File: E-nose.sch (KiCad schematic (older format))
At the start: 34 parts, among them T1 Temp_si072, U1 TCA9548APWR, U3 RTC_DS3231

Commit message: Final with Gerbers
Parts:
- removed XA2: Arduino_Due_Shield, Arduino:Arduino_Due_Shield, symbol arduino:Arduino_Due_Shield
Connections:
- wire segments 80 -> 81
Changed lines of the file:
@@
 $EndDescr
-$Comp
-L arduino:Arduino_Due_Shield XA2
-U 1 1 620C63F8
-P 6450 8400
-F 0 "XA2" H 6450 6019 60  0000 C CNN
-F 1 "Arduino_Due_Shield" H 6450 5913 60  0000 C CNN
-F 2 "Arduino:Arduino_Due_Shield" H 7150 11150 60  0001 C CNN
-F 3 "https://store.arduino.cc/arduino-due" H 7150 11150 60  0001 C CNN
-	1    6450 8400
-	1    0    0    -1
-$EndComp
 $Comp
 L Interface_Expansion:TCA9548APWR U1
@@
 	13300 1650 13350 1650
 Text GLabel 11750 3000 0    50   Input ~ 0
-SD4
+SD1
 $Comp
 L power:VCC #PWRVcc0104
@@
 	11650 2700 11800 2700
 Text GLabel 11750 2800 0    50   Input ~ 0
-SC4
+SC1
 Wire Wire Line
 	11800 3000 11750 3000
@@
 	11750 2800 11800 2800
 Text GLabel 13350 3050 0    50   Input ~ 0
-SD2
+SD3
 $Comp
 L power:VCC #PWRVcc0105
@@
 	13250 2750 13400 2750
 Text GLabel 13350 2850 0    50   Input ~ 0
-SC2
+SC3
 Wire Wire Line
 	13400 3050 13350 3050
@@
 	13350 2850 13400 2850
 Text GLabel 11750 4200 0    50   Input ~ 0
-SD1
+SD5
 $Comp
 L power:VCC #PWRVcc0106
@@
 	11650 3900 11800 3900
 Text GLabel 11750 4000 0    50   Input ~ 0
-SC1
+SC5
 Wire Wire Line
 	11800 4200 11750 4200
@@
 	11750 4000 11800 4000
 Text GLabel 13250 4200 0    50   Input ~ 0
-SD0
+SD4
 $Comp
 L power:VCC #PWRVcc0107
@@
 	1    0    0    -1
 $EndComp
-$Comp
-L Jumper:SolderJumper_2_Open JP12
-U 1 1 62169236
-P 13100 3650
-F 0 "JP12" H 13100 3855 50  0000 C CNN
-F 1 "SolderJumper_2_Open" H 13100 3764 50  0001 C CNN
-F 2 "Jumper:SolderJumper-2_P1.3mm_Open_RoundedPad1.0x1.5mm" H 13100 3650 50  0001 C CNN
-F 3 "~" H 13100 3650 50  0001 C CNN
-	1    13100 3650
-	0    -1   -1   0
-$EndComp
 Wire Wire Line
 	13100 3500 13300 3500
@@
 	13150 3900 13300 3900
 Text GLabel 13250 4000 0    50   Input ~ 0
-SC0
+SC4
 Wire Wire Line
 	13300 4200 13250 4200
@@
 	13250 4000 13300 4000
 Text GLabel 14900 1950 0    50   Input ~ 0
-SD5
+SD0
 $Comp
 L power:VCC #PWRVcc0108
@@
 	14800 1650 14950 1650
 Text GLabel 14900 1750 0    50   Input ~ 0
-SC5
+SC0
 Wire Wire Line
 	14950 1950 14900 1950
@@
 	14900 1750 14950 1750
 Text GLabel 14850 3150 0    50   Input ~ 0
-SD3
+SD2
 $Comp
 L power:VCC #PWRVcc0109
@@
 	14750 2850 14900 2850
 Text GLabel 14850 2950 0    50   Input ~ 0
-SC3
+SC2
 Wire Wire Line
 	14900 3150 14850 3150
@@
 Wire Wire Line
 	11800 3500 11800 3700
+$Comp
+L power:GND #PWR0127
+U 1 1 6217D8D2
+P 2400 5500
+F 0 "#PWR0127" H 2400 5250 50  0001 C CNN
+F 1 "GND" V 2405 5372 50  0000 R CNN
+F 2 "" H 2400 5500 50  0001 C CNN
+F 3 "" H 2400 5500 50  0001 C CNN
+	1    2400 5500
+	0    1    1    0
+$EndComp
+$Comp
+L power:+5V #PWR5V0103
+U 1 1 624CFCA8
+P 3750 1400
+F 0 "#PWR5V0103" H 3750 1250 50  0001 C CNN
+F 1 "+5V" H 3765 1573 50  0000 C CNN
+F 2 "" H 3750 1400 50  0001 C CNN
+F 3 "" H 3750 1400 50  0001 C CNN
+	1    3750 1400
+	1    0    0    -1
+$EndComp
+$Comp
+L power:GND #PWR0128
+U 1 1 624D09CB
+P 3850 1550
+F 0 "#PWR0128" H 3850 1300 50  0001 C CNN
+F 1 "GND" H 3855 1377 50  0000 C CNN
+F 2 "" H 3850 1550 50  0001 C CNN
+F 3 "" H 3850 1550 50  0001 C CNN
+	1    3850 1550
+	-1   0    0    1
+$EndComp
+Wire Wire Line
+	3750 1400 3750 1550
+$Comp
+L Jumper:SolderJumper_2_Open JP12
+U 1 1 625B1467
+P 13100 3650
+F 0 "JP12" H 13100 3855 50  0000 C CNN
+F 1 "SolderJumper_2_Open" H 13100 3764 50  0001 C CNN
+F 2 "Jumper:SolderJumper-2_P1.3mm_Open_RoundedPad1.0x1.5mm" H 13100 3650 50  0001 C CNN
+F 3 "~" H 13100 3650 50  0001 C CNN
+	1    13100 3650
+	0    -1   -1   0
+$EndComp
 $EndSCHEMATC

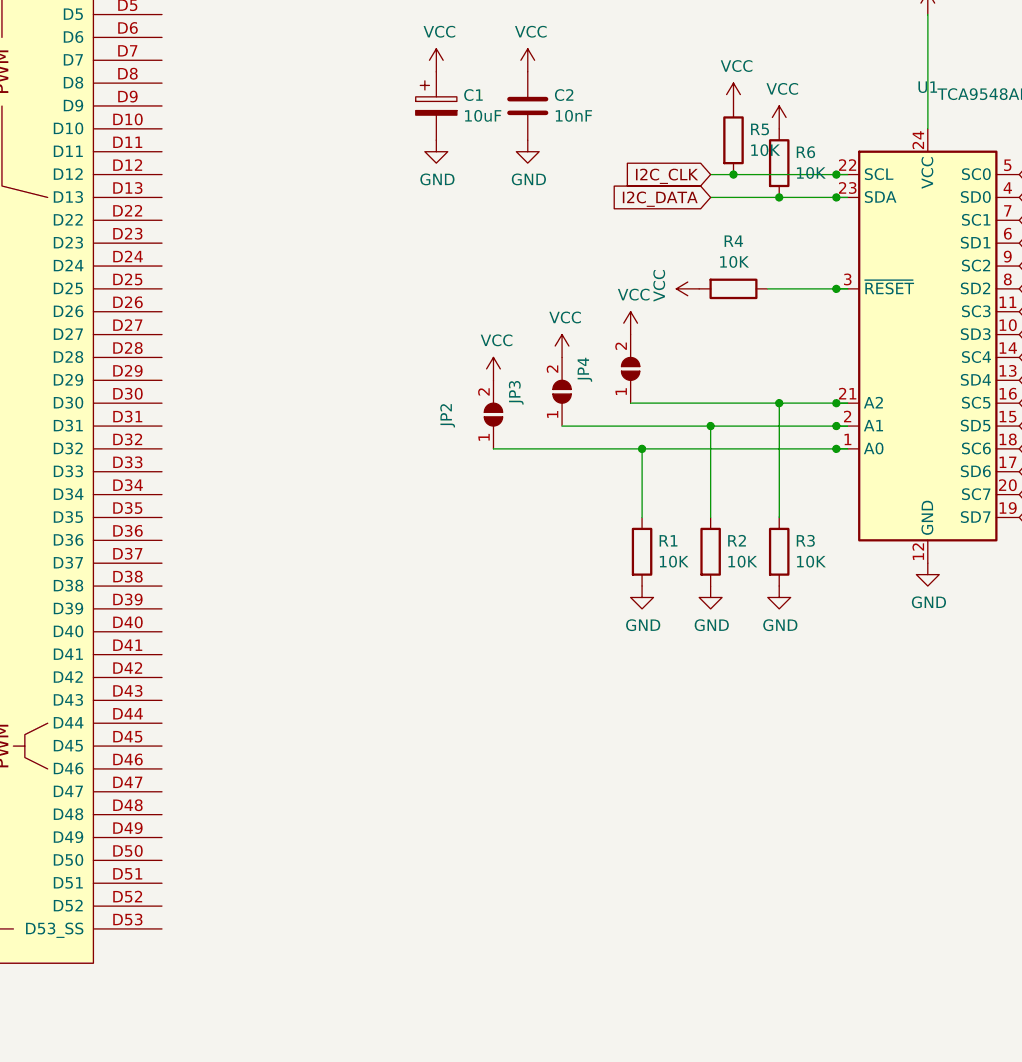
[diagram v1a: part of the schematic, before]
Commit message: Dip switch add
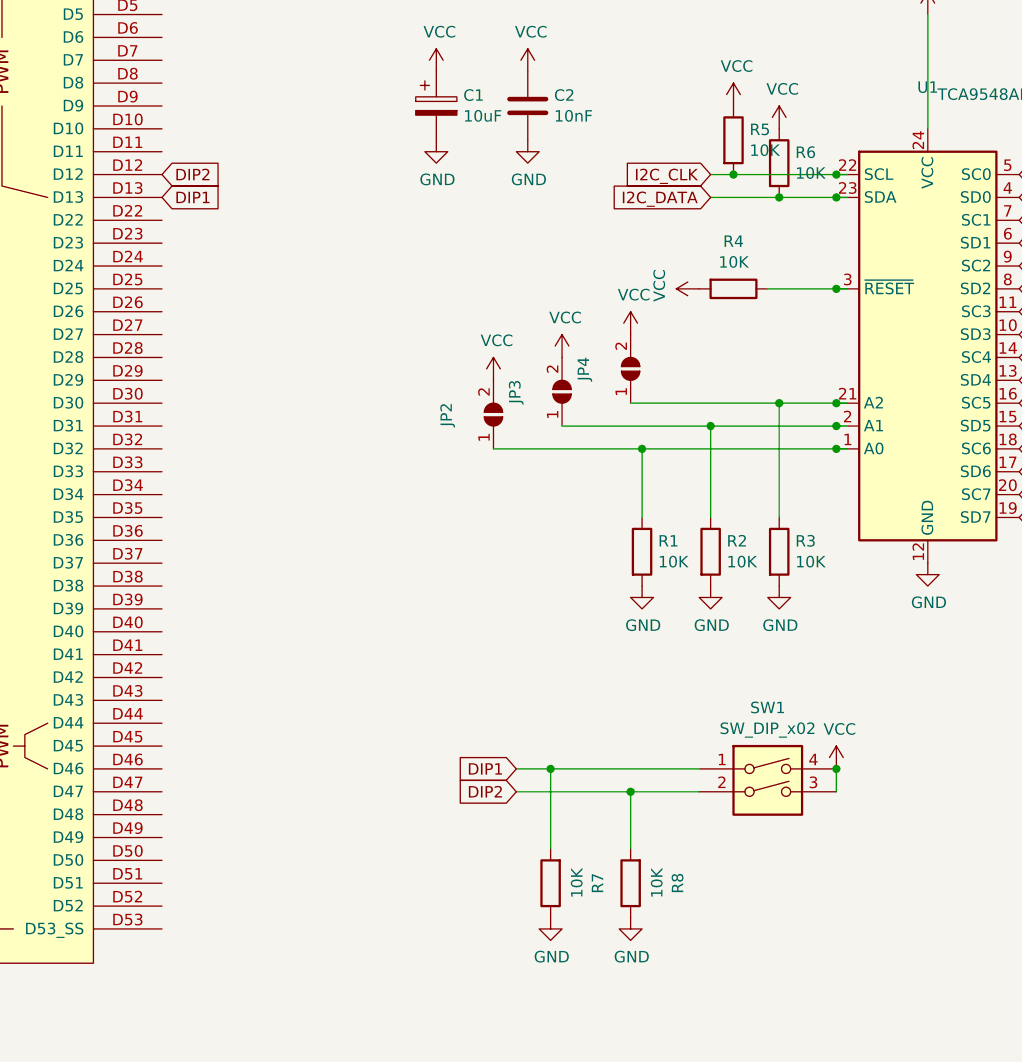
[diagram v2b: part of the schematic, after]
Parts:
- added R7, R8: 10K, Resistor_SMD:R_0805_2012Metric_Pad1.20x1.40mm_HandSolder, symbol Device:R
- added SW1: SW_DIP_x02, Button_Switch_THT:SW_DIP_SPSTx02_Slide_6.7x6.64mm_W7.62mm_P2.54mm_LowProfile, symbol Switch:SW_DIP_x02
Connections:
- net labels added: DIP1, DIP2
- wire segments 81 -> 88
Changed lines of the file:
@@
 	0    -1   -1   0
 $EndComp
+$Comp
+L Switch:SW_DIP_x02 SW1
+U 1 1 621805E0
+P 7650 5700
+F 0 "SW1" H 7650 6067 50  0000 C CNN
+F 1 "SW_DIP_x02" H 7650 5976 50  0000 C CNN
+F 2 "Button_Switch_THT:SW_DIP_SPSTx02_Slide_6.7x6.64mm_W7.62mm_P2.54mm_LowProfile" H 7650 5700 50  0001 C CNN
+F 3 "~" H 7650 5700 50  0001 C CNN
+	1    7650 5700
+	1    0    0    -1
+$EndComp
+Text GLabel 5000 3100 2    50   Input ~ 0
+DIP1
+Text GLabel 5000 3000 2    50   Input ~ 0
+DIP2
+Text GLabel 6550 5600 0    50   Input ~ 0
+DIP1
+Text GLabel 6550 5700 0    50   Input ~ 0
+DIP2
+$Comp
+L power:VCC #PWR?
+U 1 1 6218F374
+P 7950 5600
+F 0 "#PWR?" H 7950 5450 50  0001 C CNN
+F 1 "VCC" H 7965 5773 50  0000 C CNN
+F 2 "" H 7950 5600 50  0001 C CNN
+F 3 "" H 7950 5600 50  0001 C CNN
+	1    7950 5600
+	1    0    0    -1
+$EndComp
+Wire Wire Line
+	7950 5700 7950 5600
+Connection ~ 7950 5600
+$Comp
+L Device:R R7
+U 1 1 6219B7EA
+P 6700 6100
+F 0 "R7" V 6493 6100 50  0000 C CNN
+F 1 "10K" V 6584 6100 50  0000 C CNN
+F 2 "Resistor_SMD:R_0805_2012Metric_Pad1.20x1.40mm_HandSolder" V 6630 6100 50  0001 C CNN
+F 3 "~" H 6700 6100 50  0001 C CNN
+	1    6700 6100
+	-1   0    0    1
+$EndComp
+$Comp
+L power:GND #PWR?
+U 1 1 6219E73C
+P 6700 6250
+F 0 "#PWR?" H 6700 6000 50  0001 C CNN
+F 1 "GND" H 6705 6077 50  0000 C CNN
+F 2 "" H 6700 6250 50  0001 C CNN
+F 3 "" H 6700 6250 50  0001 C CNN
+	1    6700 6250
+	1    0    0    -1
+$EndComp
+Wire Wire Line
+	6550 5600 6700 5600
+Wire Wire Line
+	6550 5700 7050 5700
+$Comp
+L Device:R R8
+U 1 1 621B2709
+P 7050 6100
+F 0 "R8" V 6843 6100 50  0000 C CNN
+F 1 "10K" V 6934 6100 50  0000 C CNN
+F 2 "Resistor_SMD:R_0805_2012Metric_Pad1.20x1.40mm_HandSolder" V 6980 6100 50  0001 C CNN
+F 3 "~" H 7050 6100 50  0001 C CNN
+	1    7050 6100
+	-1   0    0    1
+$EndComp
+Wire Wire Line
+	6700 5950 6700 5600
+Connection ~ 6700 5600
+Wire Wire Line
+	6700 5600 7350 5600
+Wire Wire Line
+	7050 5950 7050 5700
+Connection ~ 7050 5700
+Wire Wire Line
+	7050 5700 7350 5700
+$Comp
+L power:GND #PWR?
+U 1 1 621BB1B6
+P 7050 6250
+F 0 "#PWR?" H 7050 6000 50  0001 C CNN
+F 1 "GND" H 7055 6077 50  0000 C CNN
+F 2 "" H 7050 6250 50  0001 C CNN
+F 3 "" H 7050 6250 50  0001 C CNN
+	1    7050 6250
+	1    0    0    -1
+$EndComp
 $EndSCHEMATC
